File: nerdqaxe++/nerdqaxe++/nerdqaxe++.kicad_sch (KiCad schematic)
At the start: 4 parts, among them J1 5.5mm/8A

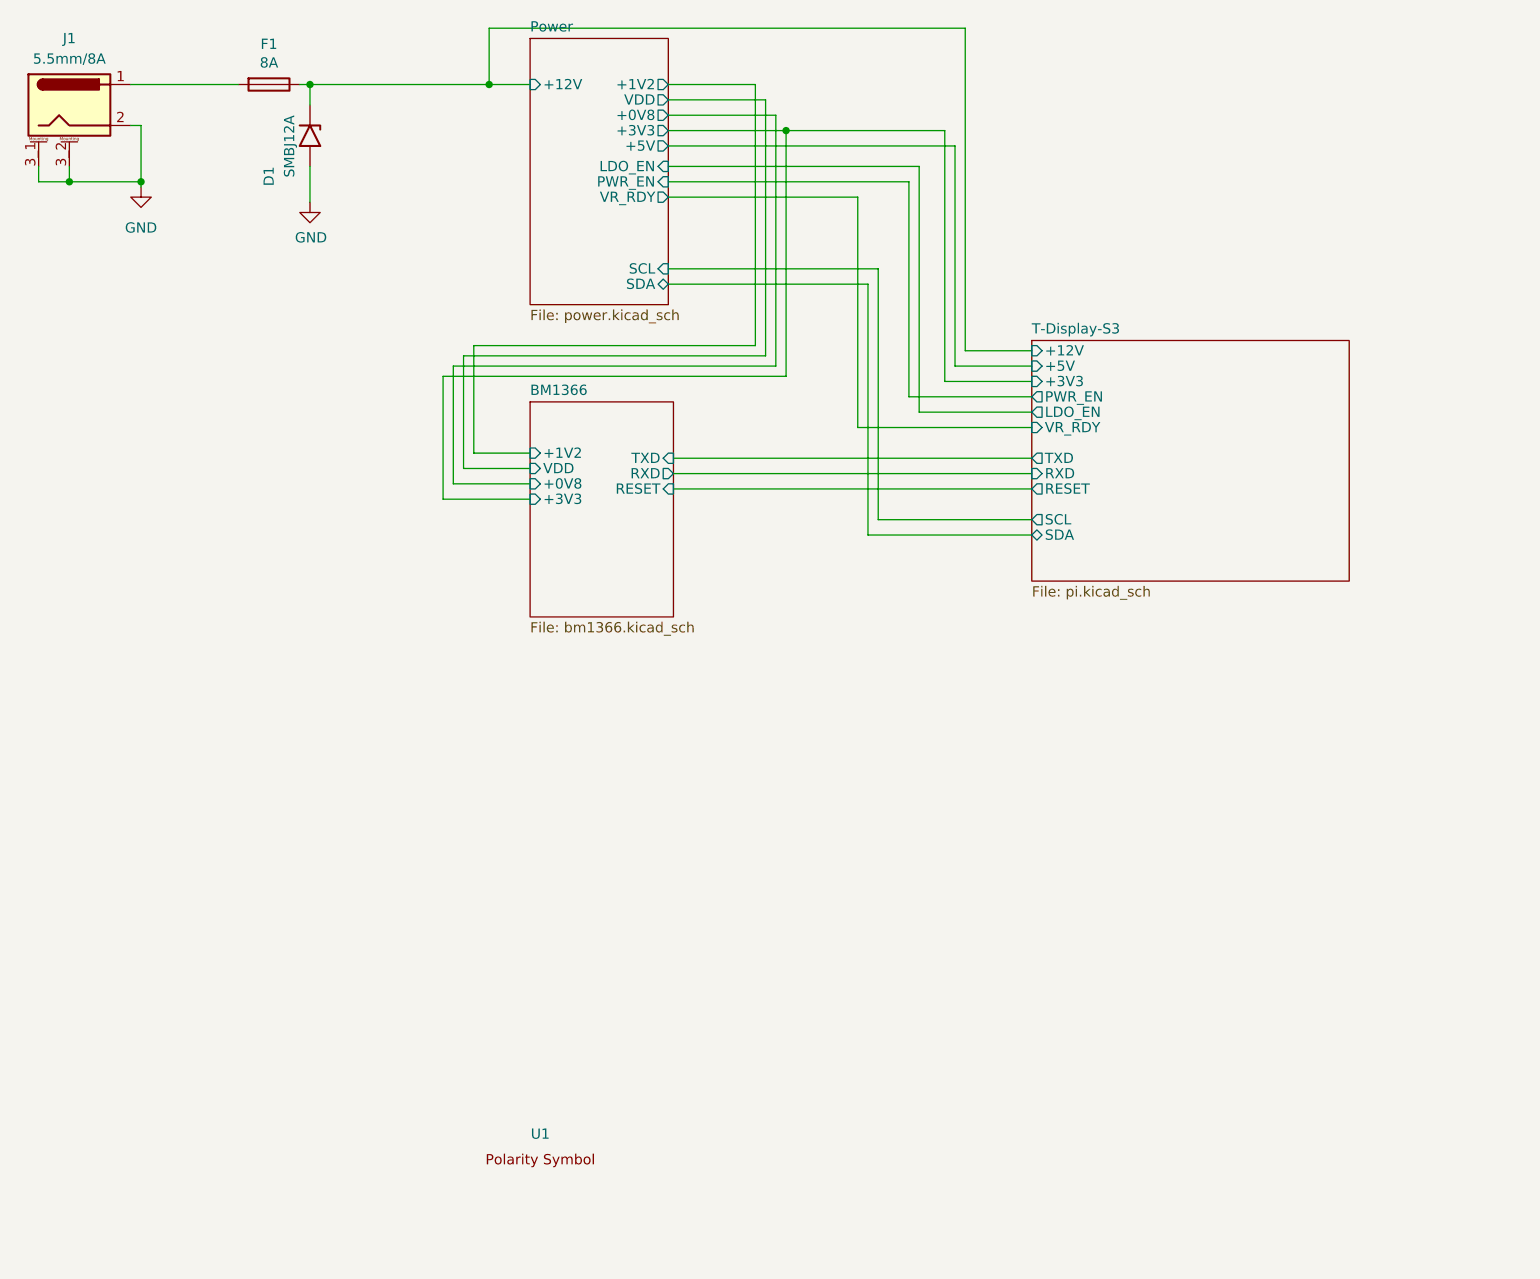
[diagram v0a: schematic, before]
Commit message: Updated PCB layout
- Replaced barrel jack socket with XT30M
- Replaced old fuse holder with new 3568
- Reordered components for AP3211 5V buck converter
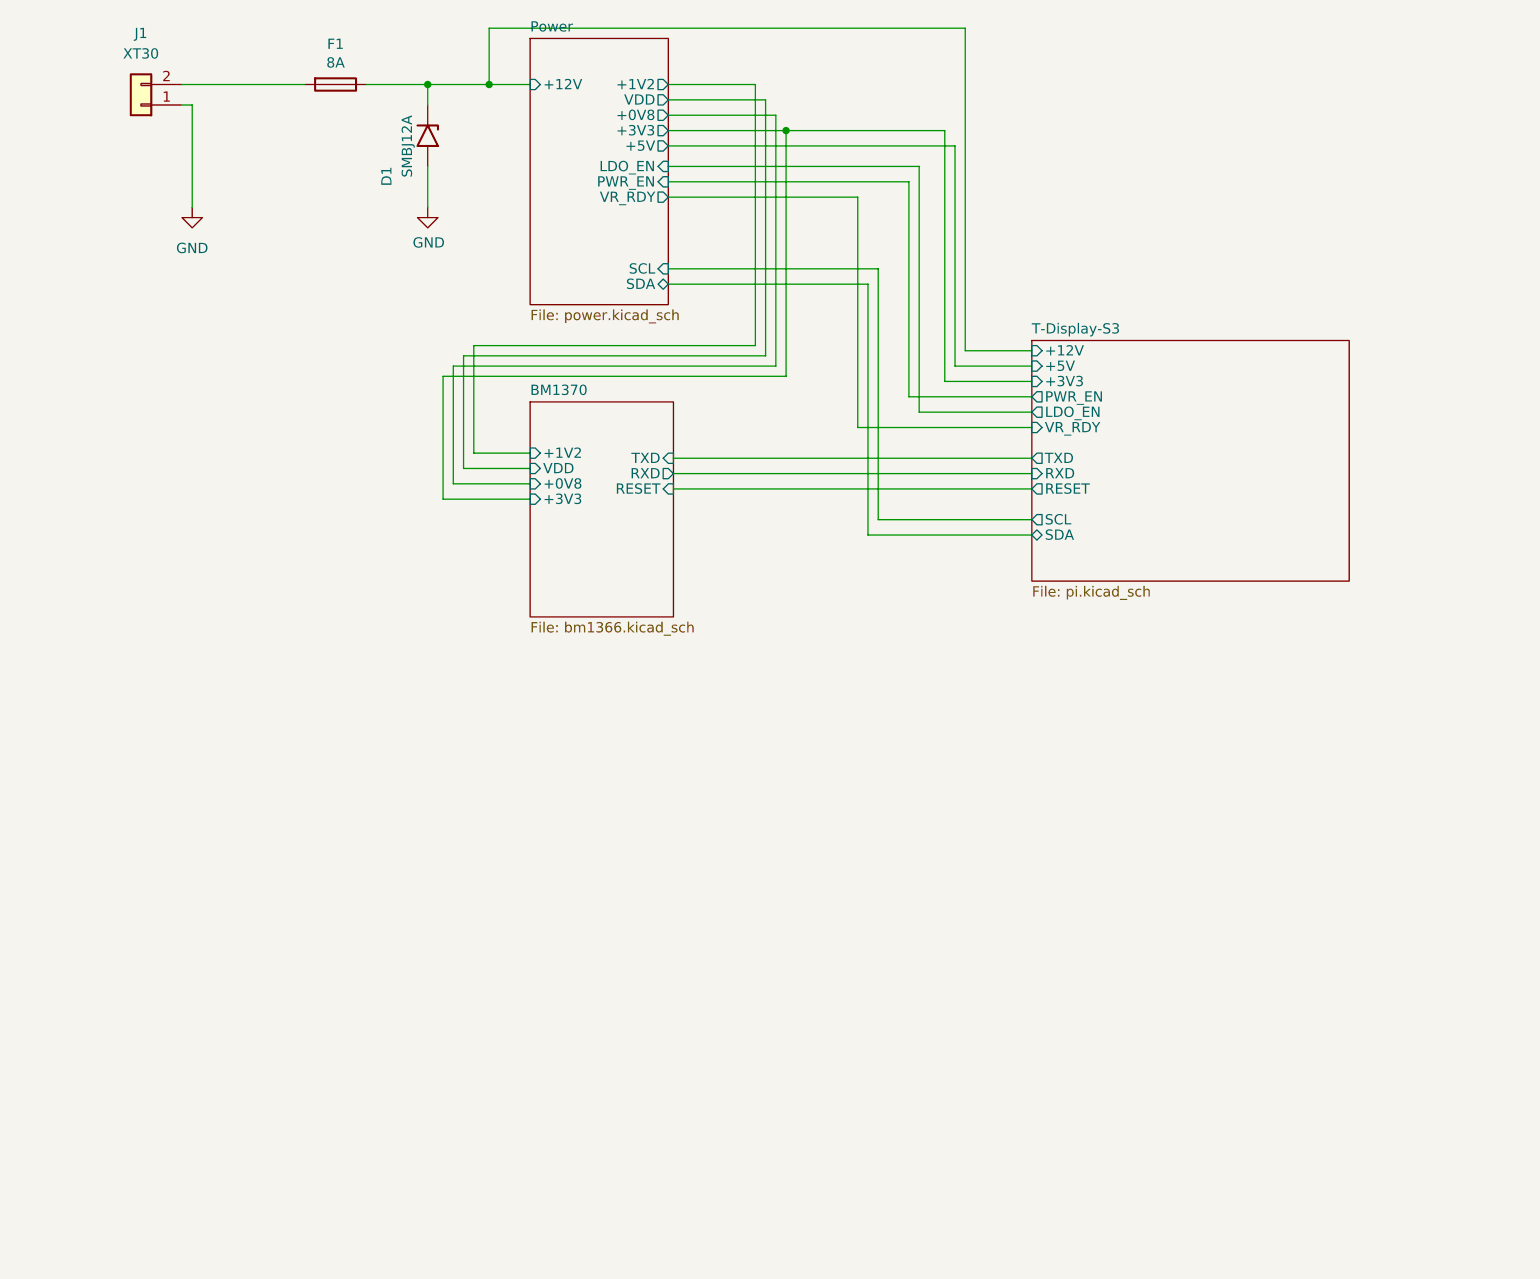
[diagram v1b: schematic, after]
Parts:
- removed J1: 5.5mm/8A, qaxe:GCT_DCJ250-20-B-XX-X_REVA1, symbol mylib7:DCJ250-20
- removed U1: ~, bitaxe:polarity, symbol bitaxe:polarity
- added J1: XT30, Connector_AMASS:AMASS_XT30PW-M_1x02_P2.50mm_Horizontal, symbol Connector_Generic:Conn_01x02
- F1: footprint myfootprints:fuseholder_littlefuse_blok -> Fuse:Fuseholder_Blade_Mini_Keystone_3568
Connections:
- net GND: now also J1.1 (Pin_1)
- net at F1.2: now also J1.2 (Pin_2)
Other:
- sheet BM1366 renamed BM1370
- moved on the sheet: D1, F1

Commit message: Nerdqaxe++ rev6.1.2PM
1. BM1370 Footprint solder paste revision
2. Added 2R2 resistor in series with bootstrap cap for CSD95472Q5MC
3. 180nH inductors for CSD
4. Vsense closer to ASICs
5. Fiducials
6. Updated top silkscreen
7. Various changes in tracing
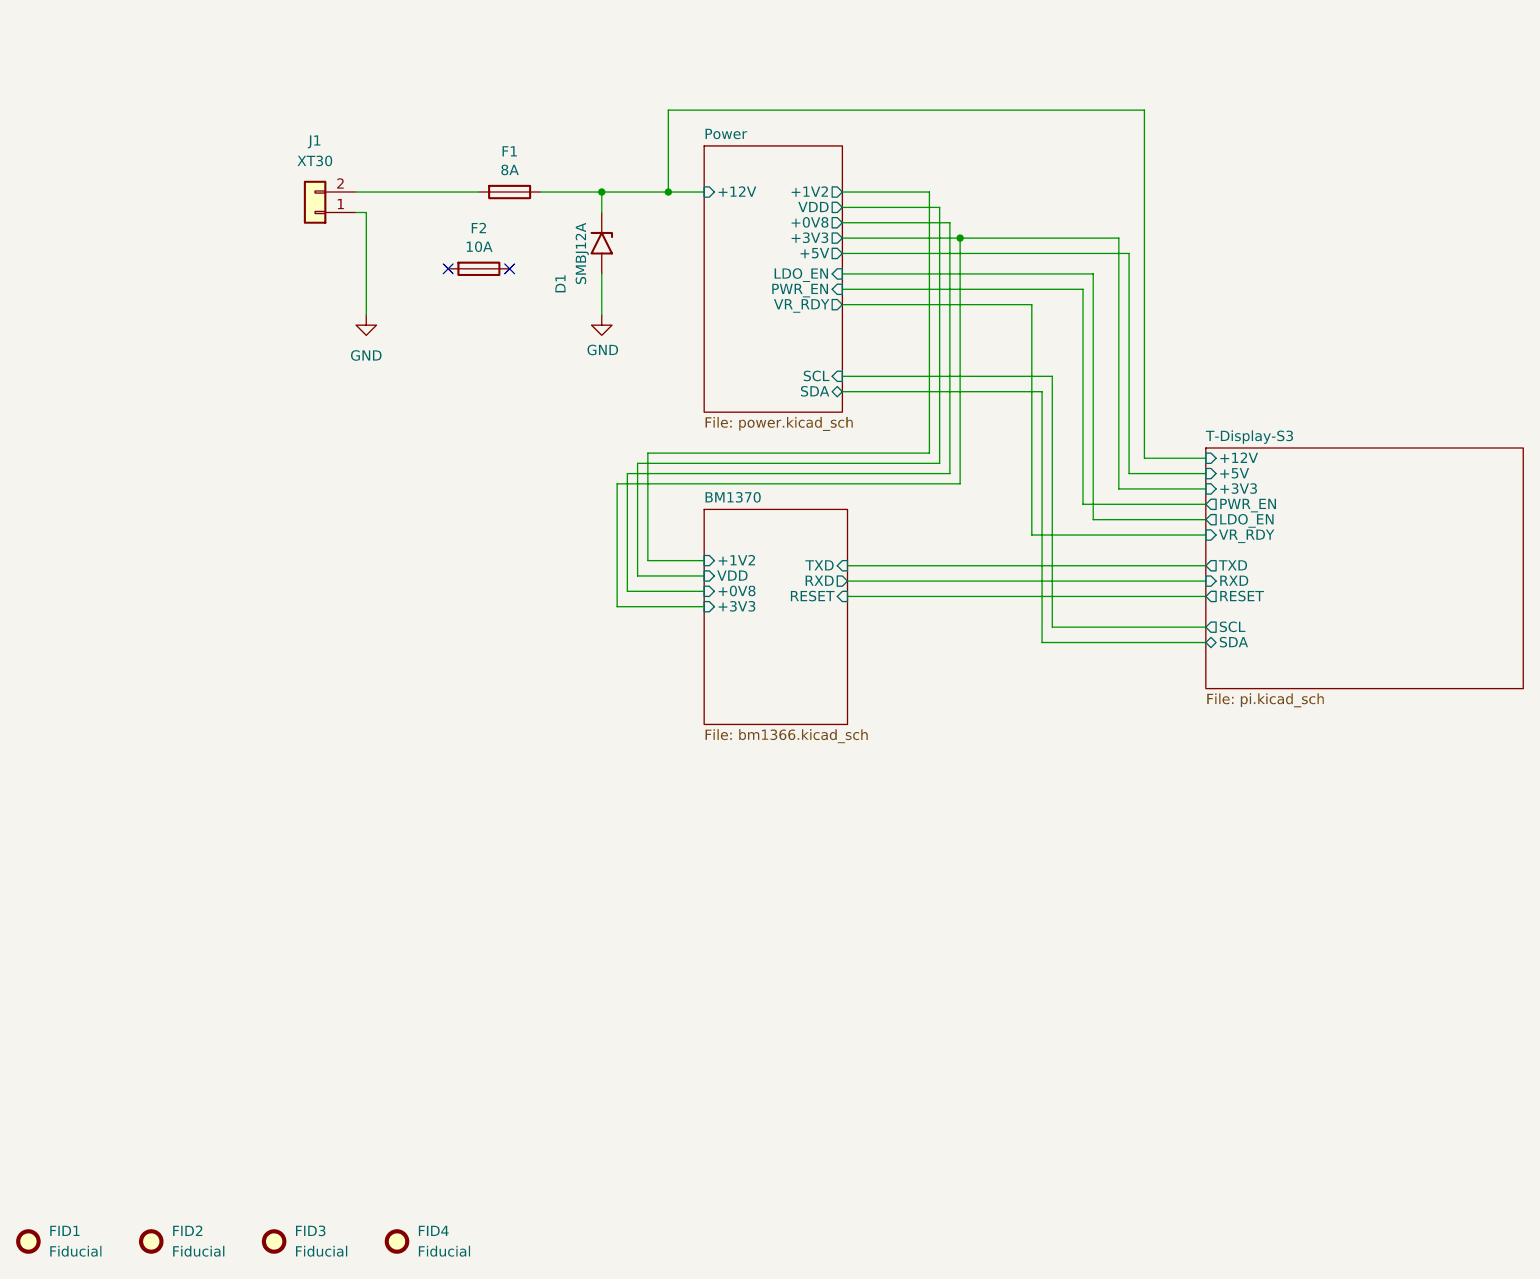
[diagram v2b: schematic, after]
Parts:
- added F2: 10A, symbol Device:Fuse
- added FID1, FID2, FID3, FID4: Fiducial, Fiducial:Fiducial_1mm_Mask2mm, symbol Mechanical:Fiducial
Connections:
- no-connect marks 0 -> 2
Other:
- moved on the sheet: D1, F1, J1
